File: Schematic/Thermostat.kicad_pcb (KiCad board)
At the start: 2 copper layers, 75 x 44 mm, 37 parts, among them J1 Relay conn., J2 Thermocouple, J3 Firmware, J4 USB_B_Micro, K1 SONGLE_SRD_05VDC_SL_C, Q1 BSS138, SW1 Reset, SW2 Temp+, SW3 Preset1, SW4 Temp-, SW5 Preset2, SW6 Function, SW7 Hysteresis, U1 MAX6675, U2 ATMEGA328P-AU, U3 Display_OLED_0.96_I2C, U4 B0505S-1WR3, Y1 16MHz

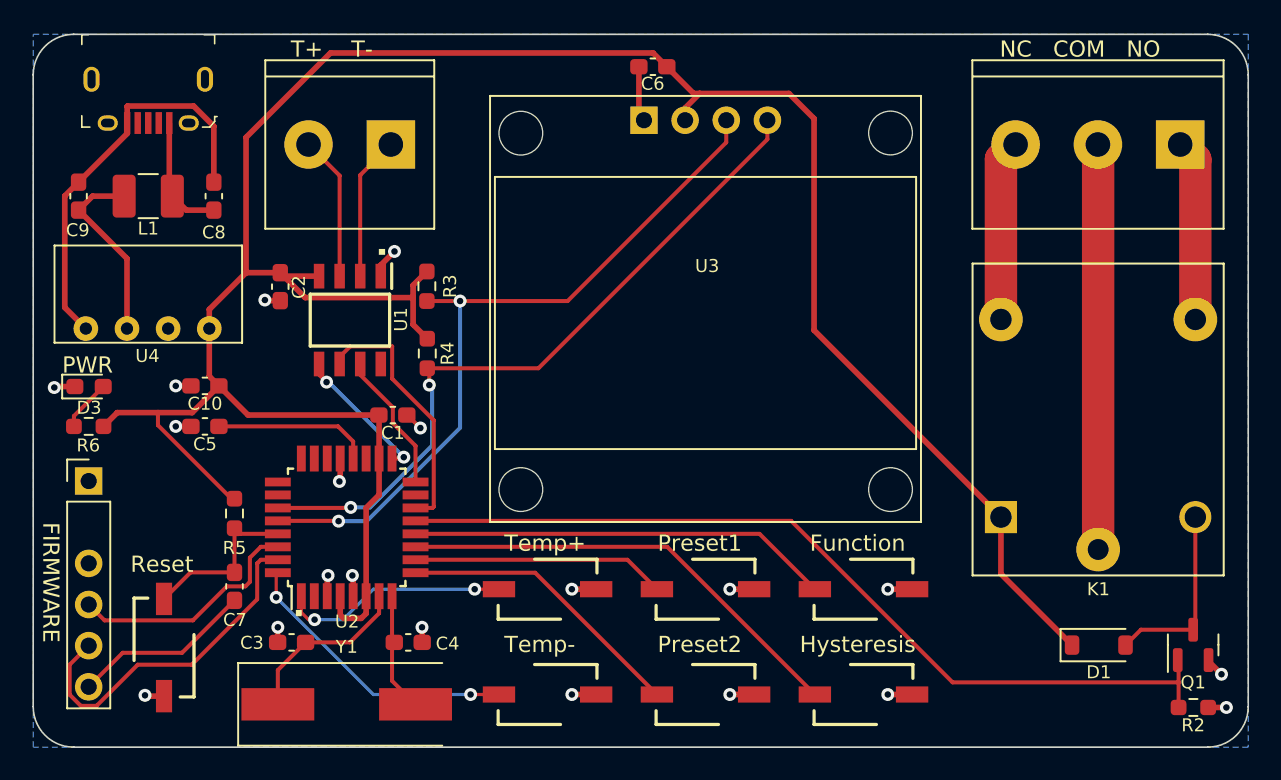
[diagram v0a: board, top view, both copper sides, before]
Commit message: Added status LEDs, changed button functions
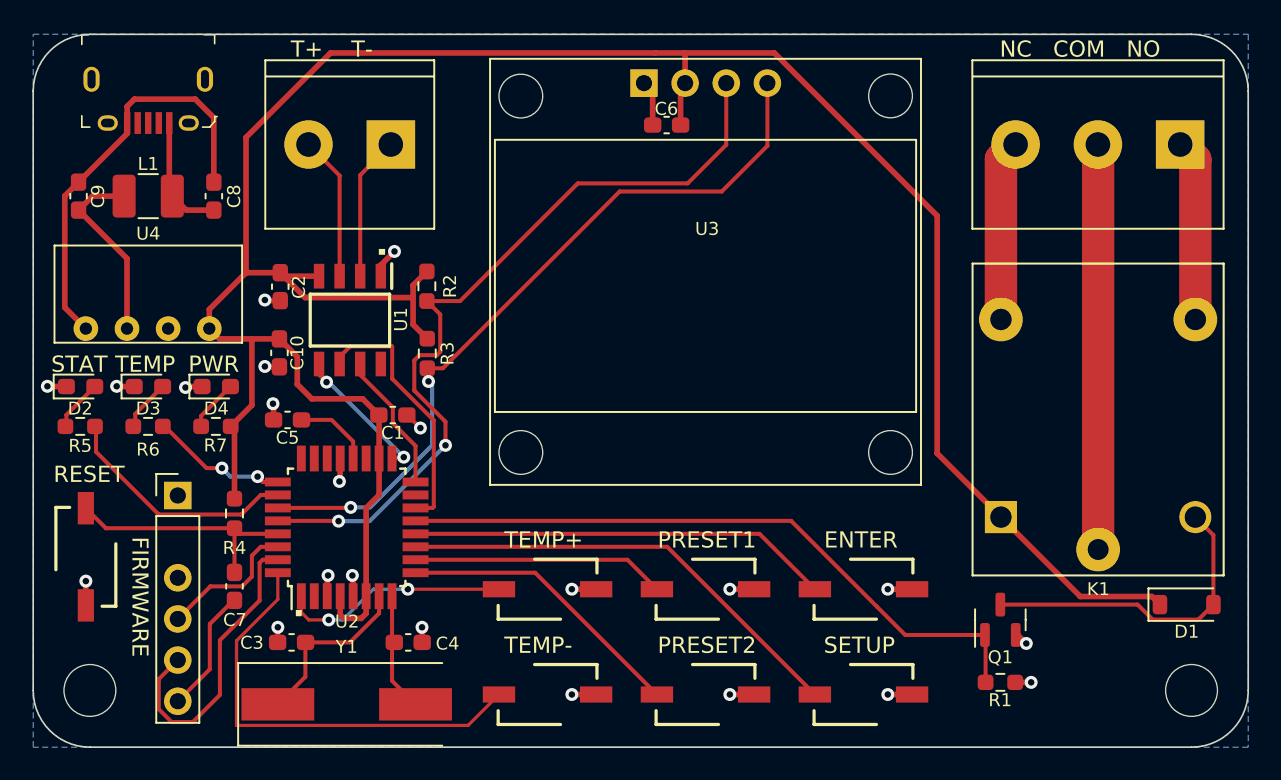
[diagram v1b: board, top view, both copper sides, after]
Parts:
- added D2: Green, LED_SMD:LED_0603_1608Metric_Pad1.05x0.95mm_HandSolder, F.Cu at (150.9, 74.7)
- added D3: Red, LED_SMD:LED_0603_1608Metric_Pad1.05x0.95mm_HandSolder, F.Cu at (155.1, 74.7)
- added H1: MountingHole, MountingHole:MountingHole_3.2mm_M3, F.Cu at (219.5, 93.5)
- added H2: MountingHole, MountingHole:MountingHole_3.2mm_M3, F.Cu at (151.5, 93.5)
- added R5: 1kΩ, Resistor_SMD:R_0603_1608Metric_Pad0.98x0.95mm_HandSolder, F.Cu at (150.9, 77.2)
- added R6: 1kΩ, Resistor_SMD:R_0603_1608Metric_Pad0.98x0.95mm_HandSolder, F.Cu at (155.1, 77.2)
- D4: renamed from D3; value "+5V" -> Green
- J3: footprint myDevices:PinHeader_1x06_P2.54mm_Vertical_Minus2 -> Retronics_Connectors:PinHeader_1x06_P2.54mm_Vertical_Minus2
- SW6: value Function -> Enter
- SW7: value Hysteresis -> Setup
- moved R1 12.0 mm to (207.7, 93.0)
- moved Q1 12.0 mm to (207.7, 89.1)
- moved D4 7.85 mm to (159.3, 74.7)
- moved R7 7.85 mm to (159.3, 77.2)
- moved SW1 7.39 mm to (151.2, 85.2)
- moved D1 5.97 mm to (219.2, 88.2)
- moved J3 5.57 mm to (156.9, 81.5)
- moved C5 5.12 mm to (163.7, 76.8)
- moved C10 5.03 mm to (163.2, 72.7), turned to 90 degrees
- moved C6 3.70 mm to (187.1, 58.6)
- moved U3 2.29 mm to (185.7, 56.0)
- renumbered R2 to R1, R3 to R2, R4 to R3, R5 to R4, R6 to R7, SW4 to SW3, SW3 to SW4
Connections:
- net SW_Function renamed SW_Enter
- net SW_Hysteresis renamed SW_Setup
- U2 pad 25: unconnected-(U2-A2-Pad25) -> LED_TEMP
- U2 pad 26: unconnected-(U2-A3-Pad26) -> LED_STATUS
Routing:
- net LED_STATUS: track 0.00 -> 14.9 mm
- net RLY_CTRL: track 54.2 -> 41.0 mm
- net SW_TEMP-: track 17.8 -> 27.5 mm, vias 2 -> 0
- net LED_TEMP: track 0.00 -> 8.40 mm, vias 0 -> 2
- net Net-(D1-A): track 11.6 -> 19.8 mm
- net Net-(J3-Pin_4): track 14.8 -> 8.77 mm
- net Net-(U2-AREF): track 9.72 -> 4.79 mm
- net Net-(U2-~{RESET}): track 10.6 -> 15.2 mm
- net SCL: track 45.4 -> 49.9 mm
- net Net-(J3-Pin_6): track 11.2 -> 7.71 mm
- net Net-(D2-A): track 0.00 -> 3.18 mm
- net Net-(D3-A): track 0.00 -> 3.16 mm
- net Net-(J3-Pin_5): track 21.7 -> 18.7 mm
- net SDA: track 44.0 -> 46.6 mm
- net GND: track 29.1 -> 30.3 mm, vias 20 -> 22
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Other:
- outline, holes or cut-outs redrawn
- board text added: "ENTER"
- board text added: "PRESET1"
- board text added: "PRESET2"
- board text added: "Programmable Thermostat R0151_2337 Bjørner Sandom"
- board text added: "RESET"
- board text added: "SETUP"
- board text added: "STAT"
- board text added: "TEMP"
- board text added: "TEMP+"
- board text added: "TEMP-"
- board text removed: "Function"
- board text removed: "Hysteresis"
- board text removed: "Preset1"
- board text removed: "Preset2"
- board text removed: "Reset"
- board text removed: "Temp+"
- board text removed: "Temp-"
- board text removed: "locked"

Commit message: Added pull-up/pull-down resistors for sensor, removed redundant LEDs
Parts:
- removed the D3 at (155.1, 74.7)
- removed the R5 at (150.9, 77.2)
- removed the R6 at (155.1, 77.2)
- added R1: 1MΩ, Resistor_SMD:R_0603_1608Metric_Pad0.98x0.95mm_HandSolder, F.Cu at (174.4, 58.3)
- added R2: 1MΩ, Resistor_SMD:R_0603_1608Metric_Pad0.98x0.95mm_HandSolder, F.Cu at (174.4, 63.5)
- added R3: 1kΩ, Resistor_SMD:R_0603_1608Metric_Pad0.98x0.95mm_HandSolder, F.Cu at (213.7, 93.0)
- D2: value Green -> Orange
- moved D2 64.7 mm to (213.7, 90.4)
- renumbered D4 to D3, R1 to R4, R2 to R5, R3 to R6, R4 to R7, R7 to R8
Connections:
- U2 pad 25: LED_TEMP -> unconnected-(U2-A2-Pad25)
- U2 pad 26: LED_STATUS -> unconnected-(U2-A3-Pad26)
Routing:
- net LED_STATUS: track 14.9 -> 0.00 mm
- net Net-(J2-Pin_2): track 8.92 -> 19.3 mm
- net LED_TEMP: track 8.40 -> 0.00 mm, vias 2 -> 0
- net RLY_CTRL: track 41.0 -> 47.5 mm
- net +5V: track 156.6 -> 162.3 mm
- net Net-(J2-Pin_1): track 8.91 -> 14.4 mm
- net Net-(D3-A) (its old number): track 3.16 -> 0.00 mm
- net Net-(D2-A): track 3.18 -> 2.62 mm
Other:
- board text added: "Programmable Thermostat R0151B_2340 Bjørner Sandom"
- board text added: "RELAY"
- board text removed: "Programmable Thermostat R0151_2337 Bjørner Sandom"
- board text removed: "STAT"
- board text removed: "TEMP"

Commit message: Altered button configuration
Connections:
- SW6 pad 1: SW_Enter -> SW_Setup
- SW7 pad 1: SW_Setup -> SW_Enter
- U2 pad 11: SW_Setup -> SW_Enter
- U2 pad 12: SW_Enter -> SW_Setup
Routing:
- net SW_Setup: track 28.4 -> 26.1 mm
- net SW_Enter: track 26.1 -> 28.4 mm
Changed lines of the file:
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@@
       (net 39 "SW_Preset1") (pinfunction "D6(PWM)") (pintype "bidirectional"))
     (pad "11" smd rect (at -1.2 4.25 180) (size 1.6 0.55) (layers "F.Cu" "F.Paste" "F.Mask")
-      (net 41 "SW_Setup") (pinfunction "D7") (pintype "bidirectional"))
+      (net 43 "SW_Enter") (pinfunction "D7") (pintype "bidirectional"))
     (pad "12" smd rect (at -0.4 4.25 180) (size 1.6 0.55) (layers "F.Cu" "F.Paste" "F.Mask")
-      (net 43 "SW_Enter") (pinfunction "D8") (pintype "bidirectional"))
+      (net 41 "SW_Setup") (pinfunction "D8") (pintype "bidirectional"))
     (pad "13" smd rect (at 0.4 4.25 180) (size 1.6 0.55) (layers "F.Cu" "F.Paste" "F.Mask")
       (net 24 "RLY_CTRL") (pinfunction "D9(PWM)") (pintype "bidirectional"))
@@
       (stroke (width 0.1) (type solid)) (layer "F.Fab"))
     (pad "1" smd rect locked (at -3 0 90) (size 1 2) (layers "F.Cu" "F.Paste" "F.Mask")
-      (net 43 "SW_Enter") (pinfunction "1") (pintype "passive"))
+      (net 41 "SW_Setup") (pinfunction "1") (pintype "passive"))
     (pad "2" smd rect locked (at 3 0 90) (size 1 2) (layers "F.Cu" "F.Paste" "F.Mask")
       (net 2 "GND") (pinfunction "2") (pintype "passive"))
@@
       (stroke (width 0.1) (type solid)) (layer "F.Fab"))
     (pad "1" smd rect (at -3 0 90) (size 1 2) (layers "F.Cu" "F.Paste" "F.Mask")
-      (net 41 "SW_Setup") (pinfunction "1") (pintype "passive"))
+      (net 43 "SW_Enter") (pinfunction "1") (pintype "passive"))
     (pad "2" smd rect (at 3 0 90) (size 1 2) (layers "F.Cu" "F.Paste" "F.Mask")
       (net 2 "GND") (pinfunction "2") (pintype "passive"))
@@
   (segment (start 186.5 93.75) (end 178.9825 86.2325) (width 0.25) (layer "F.Cu") (net 40))
   (segment (start 178.9825 86.2325) (end 171.6 86.2325) (width 0.25) (layer "F.Cu") (net 40))
-  (segment (start 187.1325 84.6325) (end 171.6 84.6325) (width 0.25) (layer "F.Cu") (net 41))
-  (segment (start 196.25 93.75) (end 187.1325 84.6325) (width 0.25) (layer "F.Cu") (net 41))
+  (segment (start 192.8325 83.8325) (end 196.25 87.25) (width 0.25) (layer "F.Cu") (net 41))
+  (segment (start 171.6 83.8325) (end 192.8325 83.8325) (width 0.25) (layer "F.Cu") (net 41))
   (segment (start 214.6125 93) (end 214.6125 90.4375) (width 0.25) (layer "F.Cu") (net 42))
   (segment (start 214.6125 90.4375) (end 214.575 90.4) (width 0.25) (layer "F.Cu") (net 42))
-  (segment (start 192.8325 83.8325) (end 196.25 87.25) (width 0.25) (layer "F.Cu") (net 43))
-  (segment (start 171.6 83.8325) (end 192.8325 83.8325) (width 0.25) (layer "F.Cu") (net 43))
+  (segment (start 187.1325 84.6325) (end 171.6 84.6325) (width 0.25) (layer "F.Cu") (net 43))
+  (segment (start 196.25 93.75) (end 187.1325 84.6325) (width 0.25) (layer "F.Cu") (net 43))
   (zone (net 2) (net_name "GND") (layer "B.Cu") (hatch edge 0.5)
     (connect_pads (clearance 0.5))

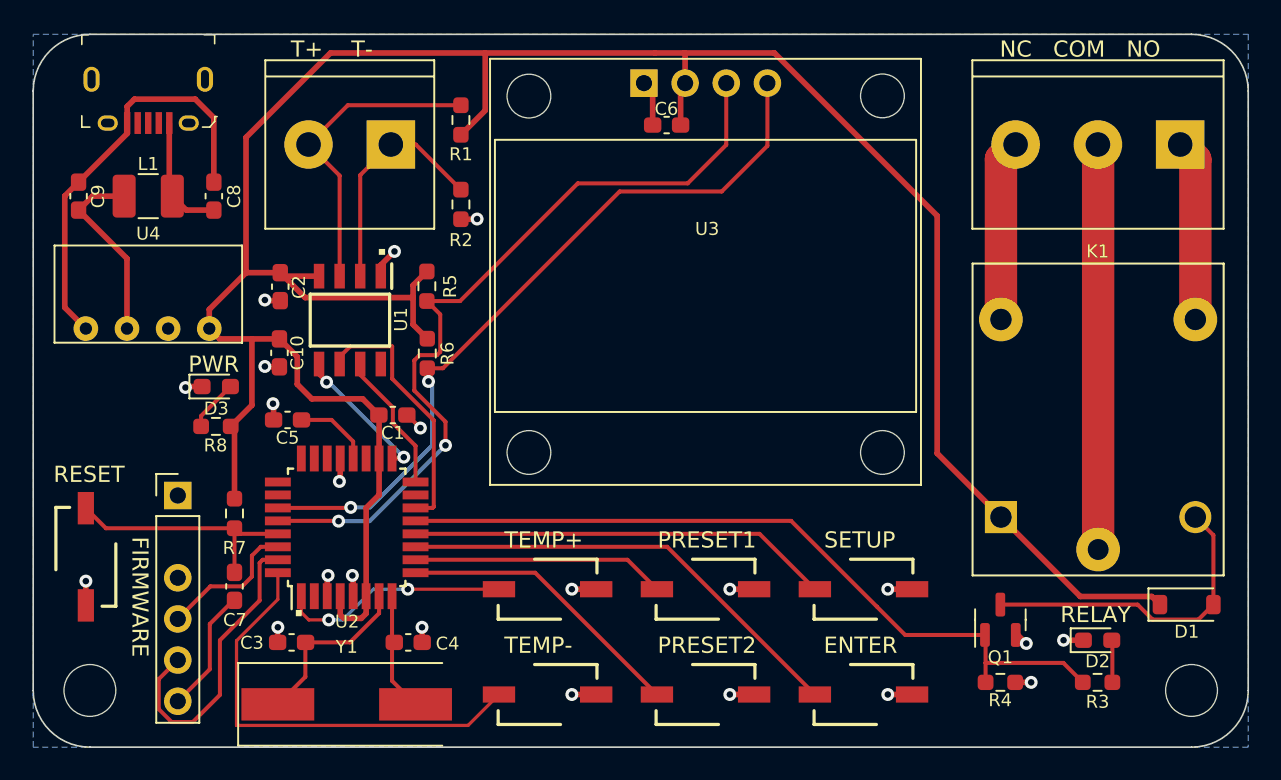
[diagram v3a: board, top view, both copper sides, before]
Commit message: Added status LEDs, rearranged buttons
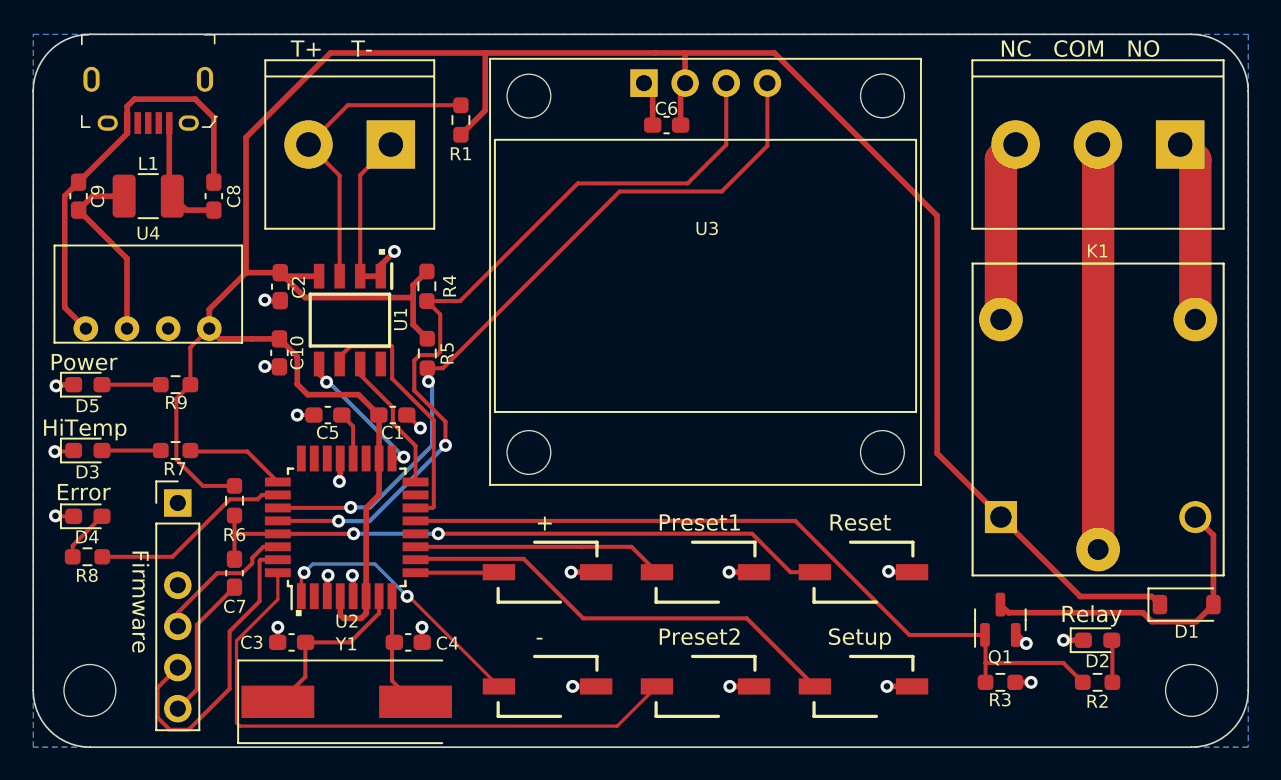
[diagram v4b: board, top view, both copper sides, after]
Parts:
- removed the R2 at (174.4, 63.5)
- removed the SW1 at (151.2, 85.2)
- added D3: Orange, LED_SMD:LED_0603_1608Metric_Pad1.05x0.95mm_HandSolder, F.Cu at (151.4, 78.7)
- added D4: Red, LED_SMD:LED_0603_1608Metric_Pad1.05x0.95mm_HandSolder, F.Cu at (151.4, 82.8)
- added R7: 1kΩ, Resistor_SMD:R_0603_1608Metric_Pad0.98x0.95mm_HandSolder, F.Cu at (156.8, 78.7)
- added R8: 1kΩ, Resistor_SMD:R_0603_1608Metric_Pad0.98x0.95mm_HandSolder, F.Cu at (151.3, 85.2)
- D2: value Orange -> Yellow
- SW3: renamed from SW6; value Enter -> Reset
- moved D5 7.93 mm to (151.4, 74.6)
- moved R9 3.58 mm to (156.8, 74.6)
- moved C5 2.51 mm to (166.2, 76.5)
- moved SW1 1.05 mm to (179.8, 86.2)
- moved SW2 1.05 mm to (189.5, 86.2)
- moved SW3 1.05 mm to (199.2, 86.2)
- moved C7 0.81 mm to (160.4, 86.3)
- moved R6 0.79 mm to (160.4, 81.8)
- moved SW4 0.50 mm to (179.8, 93.2)
- moved SW5 0.50 mm to (189.5, 93.2)
- moved SW6 0.50 mm to (199.2, 93.2)
- moved J3 0.46 mm to (156.9, 81.9)
- moved Y1 0.16 mm to (167.3, 94.2)
- renumbered D3 to D5, R3 to R2, R4 to R3, R5 to R4, R6 to R5, R7 to R6, R8 to R9, SW2 to SW1, SW4 to SW2, SW3 to SW4, SW7 to SW6
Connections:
- C7 pad 2: Net-(U2-~{RESET}) -> SW_Reset
- J2 pad 1: Net-(J2-Pin_1) -> GND
- R6 pad 2: Net-(U2-~{RESET}) -> SW_Reset
- SW1 pad 1: SW_TEMP+ -> SW_Temp+
- SW3 pad 1: SW_Setup -> SW_Reset
- SW4 pad 1: SW_TEMP- -> SW_Temp-
- SW6 pad 1: SW_Enter -> SW_Setup
- U1 pad 2: Net-(J2-Pin_1) -> GND
- U2 pad 1: SW_TEMP+ -> SW_Temp-
- U2 pad 10: SW_Preset1 -> SW_Setup
- U2 pad 11: SW_Enter -> SW_Preset1
- U2 pad 12: SW_Setup -> unconnected-(U2-D8-Pad12)
- U2 pad 25: unconnected-(U2-A2-Pad25) -> LED_HITEMP
- U2 pad 26: unconnected-(U2-A3-Pad26) -> LED_ERROR
- U2 pad 29: Net-(U2-~{RESET}) -> SW_Reset
- U2 pad 32: SW_TEMP- -> SW_Preset2
- U2 pad 9: SW_Preset2 -> SW_Temp+
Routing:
- net SW_Reset: track 0.00 -> 39.5 mm, vias 0 -> 2
- net SW_Enter: track 28.4 -> 0.00 mm
- net SW_TEMP-: track 27.5 -> 0.00 mm
- net SW_Preset2: track 18.0 -> 37.4 mm
- net SW_Temp-: track 0.00 -> 16.9 mm, vias 0 -> 2
- net Net-(U2-~{RESET}): track 15.2 -> 0.00 mm
- net Net-(J2-Pin_1): track 14.4 -> 0.00 mm
- net SW_TEMP+: track 14.2 -> 0.00 mm, vias 2 -> 0
- net LED_ERROR: track 0.00 -> 12.4 mm
- net GND: track 30.3 -> 40.3 mm
- net LED_HITEMP: track 0.00 -> 6.18 mm
- net SW_Temp+: track 0.00 -> 5.16 mm
- net Net-(D3-A): track 0.00 -> 3.65 mm
- net Net-(D4-A): track 0.00 -> 3.25 mm
- net +5V: track 162.3 -> 165.0 mm
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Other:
- board text added: "+"
- board text added: "-"
- board text added: "Error"
- board text added: "Firmware"
- board text added: "HiTemp"
- board text added: "Power"
- board text added: "Preset1"
- board text added: "Preset2"
- board text added: "Programmable Thermostat R0151C_2342 Bjørner Sandom"
- board text added: "Relay"
- board text added: "Reset"
- board text added: "Setup"
- board text removed: "ENTER"
- board text removed: "FIRMWARE"
- board text removed: "PRESET1"
- board text removed: "PRESET2"
- board text removed: "PWR"
- board text removed: "Programmable Thermostat R0151B_2340 Bjørner Sandom"
- board text removed: "RELAY"
- board text removed: "RESET"
- board text removed: "SETUP"
- board text removed: "TEMP+"
- board text removed: "TEMP-"
